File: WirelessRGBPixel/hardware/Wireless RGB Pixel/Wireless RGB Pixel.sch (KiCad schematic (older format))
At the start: 7 parts

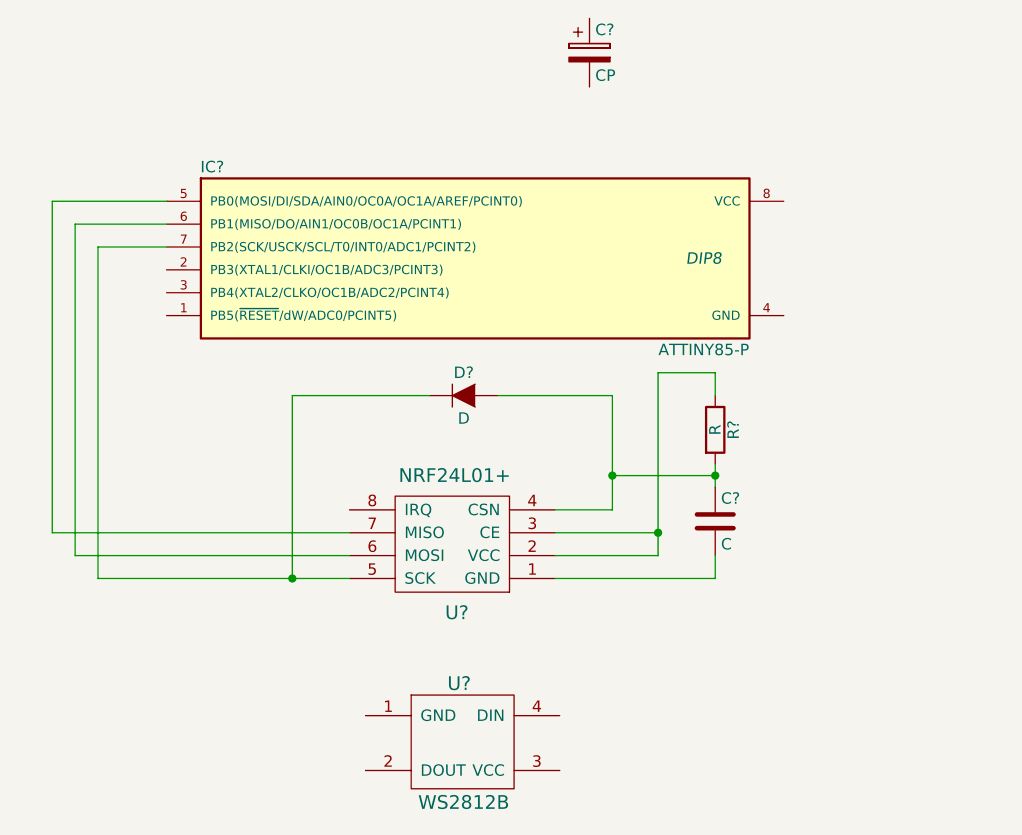
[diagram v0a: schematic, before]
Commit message: First shot at Wireless Pixel PCB
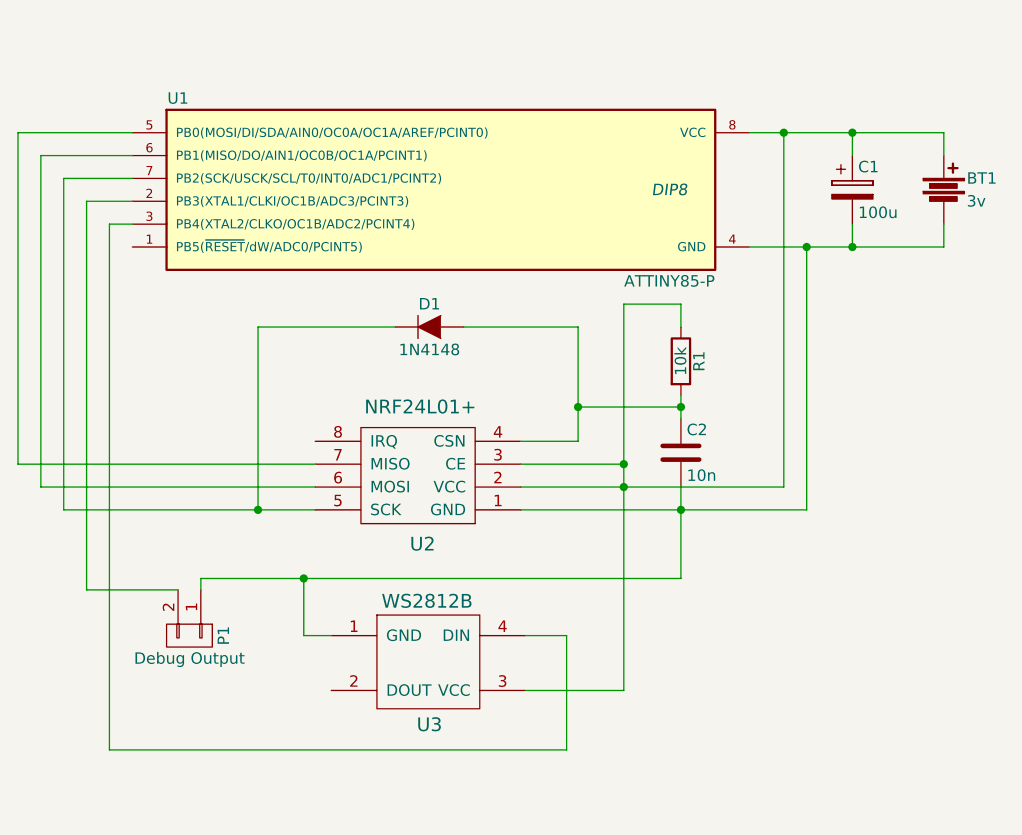
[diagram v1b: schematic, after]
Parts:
- removed U?: WS2812B, symbol WS2812B
- added BT1: 3v, Pin_Headers:Pin_Header_Straight_1x02, symbol Battery
- added P1: Debug Output, Pin_Headers:Pin_Header_Straight_1x02, symbol CONN_01X02
- added U3: WS2812B, Pin_Headers:Pin_Header_Straight_1x03, symbol WS2812B-RESCUE-Wireless_RGB_Pixel
- C1: renamed from C?; value CP -> 100u; footprint (none) -> Capacitors_ThroughHole:C_Radial_D5_L11_P2
- C2: renamed from C?; value C -> 10n; footprint (none) -> Capacitors_ThroughHole:C_Disc_D6_P5
- D1: renamed from D?; value D -> 1N4148; footprint (none) -> Diodes_ThroughHole:Diode_DO-41_SOD81_Vertical_KathodeUp
- R1: renamed from R?; value R -> 10k; footprint (none) -> Resistors_ThroughHole:Resistor_Cement_Vertical_KOA-BGR-5N-7N
- gave numbers to parts that had none: 2
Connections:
- net at U1.2 (PB3(XTAL1/CLKI/OC1B/ADC3/PCINT3)): now also P1.2 (P2)
- net at U1.3 (PB4(XTAL2/CLKO/OC1B/ADC2/PCINT4)): now also U3.4 (DIN)
- net at U1.4 (GND): now also C1.2, C2.2, U2.1 (GND), BT1.2, P1.1 (P1), U3.1 (GND)
- net at U1.8 (VCC): now also C1.1, R1.1, U2.2 (VCC), U2.3 (CE), BT1.1, U3.3 (VCC)
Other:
- moved on the sheet: C1, C2, D1, R1, U1, U2
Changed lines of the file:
@@
 EESchema Schematic File Version 2
+LIBS:Wireless RGB Pixel-rescue
 LIBS:power
 LIBS:device
@@
 encoding utf-8
 Sheet 1 1
-Title ""
-Date ""
-Rev ""
+Title "Wireless RGB Pixel"
+Date "2016-07-09"
+Rev "1"
 Comp ""
-Comment1 ""
-Comment2 ""
+Comment1 "Copyright Mark Benson 2016"
+Comment2 "License Creative Commons Atribution 4.0 (CC-BY 4.0)"
 Comment3 ""
 Comment4 ""
 $EndDescr
 $Comp
-L ATTINY85-P IC?
+L ATTINY85-P U1
 U 1 1 577FF051
-P 5600 2900
-F 0 "IC?" H 4450 3300 50  0000 C CNN
-F 1 "ATTINY85-P" H 6600 2500 50  0000 C CNN
-F 2 "DIP8" H 6600 2900 50  0000 C CIN
-F 3 "" H 5600 2900 50  0000 C CNN
-	1    5600 2900
-	1    0    0    -1
-$EndComp
-$Comp
-L C C?
+P 5450 2600
+F 0 "U1" H 4300 3000 50  0000 C CNN
+F 1 "ATTINY85-P" H 6450 2200 50  0000 C CNN
+F 2 "DIP8" H 6450 2600 50  0000 C CIN
+F 3 "" H 5450 2600 50  0000 C CNN
+	1    5450 2600
+	1    0    0    -1
+$EndComp
+$Comp
+L C C2
 U 1 1 577FF0D9
-P 6650 4050
-F 0 "C?" H 6675 4150 50  0000 L CNN
-F 1 "C" H 6675 3950 50  0000 L CNN
-F 2 "" H 6688 3900 50  0000 C CNN
-F 3 "" H 6650 4050 50  0000 C CNN
-	1    6650 4050
-	1    0    0    -1
-$EndComp
-$Comp
-L CP C?
+P 6500 3750
+F 0 "C2" H 6525 3850 50  0000 L CNN
+F 1 "10n" H 6525 3650 50  0000 L CNN
+F 2 "Capacitors_ThroughHole:C_Disc_D6_P5" H 6538 3600 50  0001 C CNN
+F 3 "" H 6500 3750 50  0000 C CNN
+	1    6500 3750
+	1    0    0    -1
+$EndComp
+$Comp
+L CP C1
 U 1 1 577FF120
-P 6100 2000
-F 0 "C?" H 6125 2100 50  0000 L CNN
-F 1 "CP" H 6125 1900 50  0000 L CNN
-F 2 "" H 6138 1850 50  0000 C CNN
-F 3 "" H 6100 2000 50  0000 C CNN
-	1    6100 2000
-	1    0    0    -1
-$EndComp
-$Comp
-L R R?
+P 7250 2600
+F 0 "C1" H 7275 2700 50  0000 L CNN
+F 1 "100u" H 7275 2500 50  0000 L CNN
+F 2 "Capacitors_ThroughHole:C_Radial_D5_L11_P2" H 7288 2450 50  0001 C CNN
+F 3 "" H 7250 2600 50  0000 C CNN
+	1    7250 2600
+	1    0    0    -1
+$EndComp
+$Comp
+L R R1
 U 1 1 577FF166
-P 6650 3650
-F 0 "R?" V 6730 3650 50  0000 C CNN
-F 1 "R" V 6650 3650 50  0000 C CNN
-F 2 "" V 6580 3650 50  0000 C CNN
-F 3 "" H 6650 3650 50  0000 C CNN
-	1    6650 3650
-	1    0    0    -1
-$EndComp
-$Comp
-L D D?
+P 6500 3350
+F 0 "R1" V 6580 3350 50  0000 C CNN
+F 1 "10k" V 6500 3350 50  0000 C CNN
+F 2 "Resistors_ThroughHole:Resistor_Cement_Vertical_KOA-BGR-5N-7N" V 6430 3350 50  0001 C CNN
+F 3 "" H 6500 3350 50  0000 C CNN
+	1    6500 3350
+	1    0    0    -1
+$EndComp
+$Comp
+L D D1
 U 1 1 577FF1AF
-P 5550 3500
-F 0 "D?" H 5550 3600 50  0000 C CNN
-F 1 "D" H 5550 3400 50  0000 C CNN
-F 2 "" H 5550 3500 50  0000 C CNN
-F 3 "" H 5550 3500 50  0000 C CNN
-	1    5550 3500
-	1    0    0    -1
-$EndComp
-$Comp
-L WS2812B U?
-U 1 1 577FF435
-P 5550 5000
-F 0 "U?" H 5530 5240 60  0000 C CNN
-F 1 "WS2812B" H 5550 4720 60  0000 C CNN
-F 2 "" H 5430 5040 60  0000 C CNN
-F 3 "" H 5430 5040 60  0000 C CNN
-	1    5550 5000
-	1    0    0    -1
-$EndComp
-Wire Wire Line
-	5950 4300 6650 4300
-Wire Wire Line
-	5950 4200 6400 4200
-Wire Wire Line
-	6400 4200 6400 3400
-Wire Wire Line
-	6400 3400 6650 3400
-Wire Wire Line
-	6650 4300 6650 4200
-Wire Wire Line
-	6650 3400 6650 3500
-Wire Wire Line
-	6650 3800 6650 3900
-Wire Wire Line
-	5950 4100 6400 4100
-Connection ~ 6400 4100
-Wire Wire Line
-	6200 4000 5950 4000
-Wire Wire Line
-	6200 3500 6200 4000
-Wire Wire Line
-	6200 3850 6650 3850
-Connection ~ 6650 3850
-Wire Wire Line
-	6200 3500 5700 3500
-Connection ~ 6200 3850
-$Comp
-L NRF24L01+ U?
+P 5400 3200
+F 0 "D1" H 5400 3300 50  0000 C CNN
+F 1 "1N4148" H 5400 3100 50  0000 C CNN
+F 2 "Diodes_ThroughHole:Diode_DO-41_SOD81_Vertical_KathodeUp" H 5400 3200 50  0001 C CNN
+F 3 "" H 5400 3200 50  0000 C CNN
+	1    5400 3200
+	1    0    0    -1
+$EndComp
+$Comp
+L NRF24L01+ U2
 U 1 1 578038B0
-P 5950 4300
-F 0 "U?" H 6380 4450 60  0000 C CNN
-F 1 "NRF24L01+" H 6390 3850 60  0000 C CNN
-F 2 "" H 5950 4310 60  0000 C CNN
-F 3 "" H 5950 4310 60  0000 C CNN
-	1    5950 4300
+P 5800 4000
+F 0 "U2" H 6230 4150 60  0000 C CNN
+F 1 "NRF24L01+" H 6240 3550 60  0000 C CNN
+F 2 "" H 5800 4010 60  0001 C CNN
+F 3 "" H 5800 4010 60  0000 C CNN
+	1    5800 4000
 	-1   0    0    1
 $EndComp
-Wire Wire Line
-	5400 3500 4800 3500
-Wire Wire Line
-	4800 3500 4800 4300
-Wire Wire Line
-	3950 4300 5050 4300
-Wire Wire Line
-	3950 4300 3950 2850
-Wire Wire Line
-	3950 2850 4250 2850
-Connection ~ 4800 4300
-Wire Wire Line
-	4250 2750 3850 2750
-Wire Wire Line
-	3850 2750 3850 4200
-Wire Wire Line
-	3850 4200 5050 4200
-Wire Wire Line
-	4250 2650 3750 2650
-Wire Wire Line
-	3750 2650 3750 4100
-Wire Wire Line
-	3750 4100 5050 4100
+$Comp
+L WS2812B-RESCUE-Wireless_RGB_Pixel U3
+U 1 1 57803B0F
+P 5400 4650
+F 0 "U3" H 5400 4360 60  0000 C CNN
+F 1 "WS2812B" H 5390 4900 60  0000 C CNN
+F 2 "Pin_Headers:Pin_Header_Straight_1x03" H 5720 4580 60  0001 C CNN
+F 3 "" H 5720 4580 60  0000 C CNN
+	1    5400 4650
+	1    0    0    -1
+$EndComp
+$Comp
+L CONN_01X02 P1
+U 1 1 57803DD6
+P 4350 4550
+F 0 "P1" H 4350 4700 50  0000 C CNN
+F 1 "Debug Output" V 4450 4550 50  0000 C CNN
+F 2 "Pin_Headers:Pin_Header_Straight_1x02" H 4350 4550 50  0001 C CNN
+F 3 "" H 4350 4550 50  0000 C CNN
+	1    4350 4550
+	0    1    1    0
+$EndComp
+$Comp
+L Battery BT1
+U 1 1 578269B4
+P 7650 2600
+F 0 "BT1" H 7750 2650 50  0000 L CNN
+F 1 "3v" H 7750 2550 50  0000 L CNN
+F 2 "Pin_Headers:Pin_Header_Straight_1x02" V 7650 2640 50  0001 C CNN
+F 3 "" V 7650 2640 50  0000 C CNN
+	1    7650 2600
+	1    0    0    -1
+$EndComp
+Wire Wire Line
+	5800 4000 7050 4000
+Wire Wire Line
+	5800 3900 6950 3900
+Wire Wire Line
+	6250 3100 6250 4790
+Wire Wire Line
+	6250 3100 6500 3100
+Wire Wire Line
+	6500 4300 6500 3900
+Wire Wire Line
+	6500 3100 6500 3200
+Wire Wire Line
+	6500 3500 6500 3600
+Wire Wire Line
+	5800 3800 6250 3800
+Connection ~ 6250 3800
+Wire Wire Line
+	6050 3700 5800 3700
+Wire Wire Line
+	6050 3200 6050 3700
+Wire Wire Line
+	6050 3550 6500 3550
+Connection ~ 6500 3550
+Wire Wire Line
+	6050 3200 5550 3200
+Connection ~ 6050 3550
+Wire Wire Line
+	5250 3200 4650 3200
+Wire Wire Line
+	4650 3200 4650 4000
+Wire Wire Line
+	3800 4000 4900 4000
+Wire Wire Line
+	3800 4000 3800 2550
+Wire Wire Line
+	3800 2550 4100 2550
+Connection ~ 4650 4000
+Wire Wire Line
+	4100 2450 3700 2450
+Wire Wire Line
+	3700 2450 3700 3900
+Wire Wire Line
+	3700 3900 4900 3900
+Wire Wire Line
+	4100 2350 3600 2350
+Wire Wire Line
+	3600 2350 3600 3800
+Wire Wire Line
+	3600 3800 4900 3800
+Connection ~ 6250 3900
+Wire Wire Line
+	4400 4300 6500 4300
+Connection ~ 6500 4000
+Wire Wire Line
+	4100 2750 4000 2750
+Wire Wire Line
+	4000 2750 4000 5050
+Wire Wire Line
+	4000 5050 6000 5050
+Wire Wire Line
+	6000 5050 6000 4550
+Wire Wire Line
+	7050 4000 7050 2850
+Wire Wire Line
+	6800 2850 7650 2850
+Wire Wire Line
+	6950 3900 6950 2350
+Wire Wire Line
+	6800 2350 7650 2350
+Wire Wire Line
+	7250 2350 7250 2450
+Connection ~ 6950 2350
+Wire Wire Line
+	7250 2850 7250 2750
+Connection ~ 7050 2850
+Wire Wire Line
+	4400 4350 4400 4300
+Connection ~ 4850 4300
+Wire Wire Line
+	4300 4350 3900 4350
+Wire Wire Line
+	3900 4350 3900 2650
+Wire Wire Line
+	3900 2650 4100 2650
+Wire Wire Line
+	7650 2350 7650 2450
+Connection ~ 7250 2350
+Wire Wire Line
+	7650 2850 7650 2750
+Connection ~ 7250 2850
+Wire Wire Line
+	4850 4300 4850 4550
+Wire Wire Line
+	4850 4550 4970 4550
+Wire Wire Line
+	6000 4550 5820 4550
+Wire Wire Line
+	6250 4790 5820 4790
 $EndSCHEMATC
